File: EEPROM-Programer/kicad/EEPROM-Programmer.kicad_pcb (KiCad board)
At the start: 2 copper layers, 100 x 60 mm, 9 parts

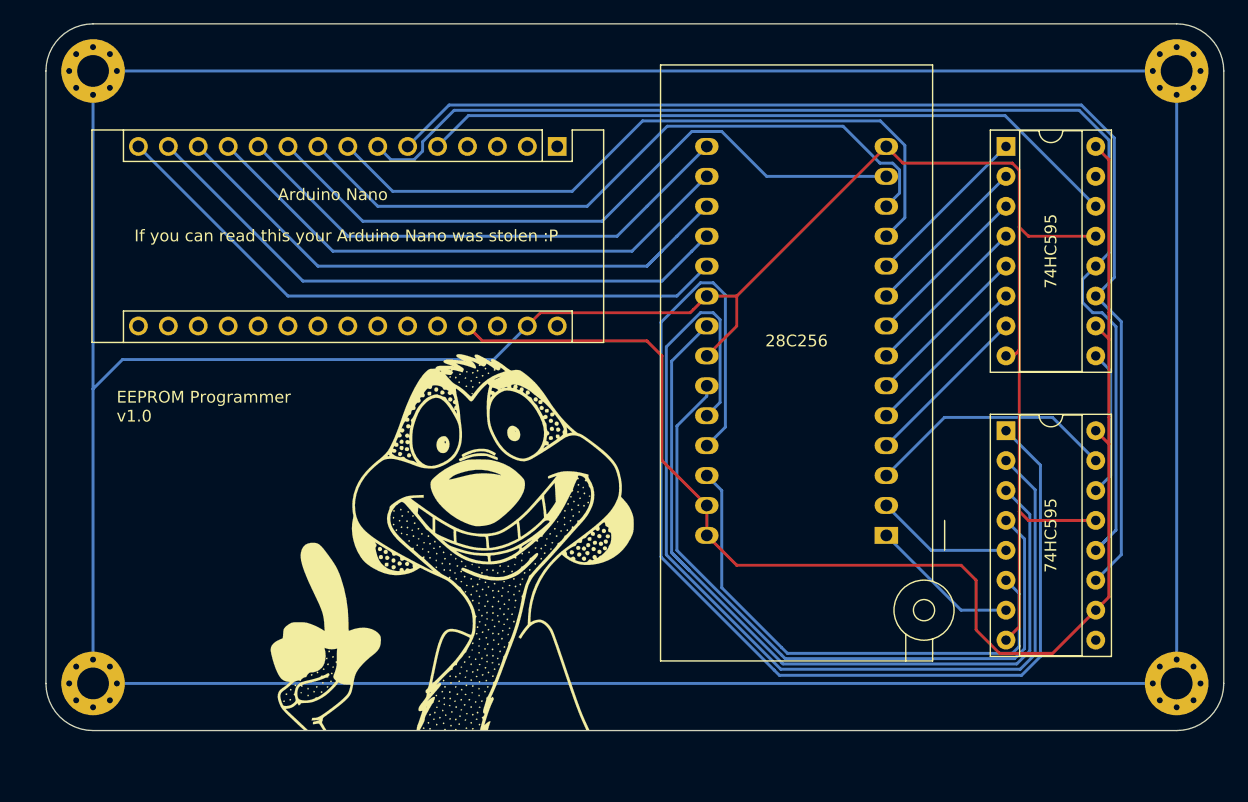
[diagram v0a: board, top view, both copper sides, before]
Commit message: EEPROM Programmer: New circuit, with more flexibility
Redesigned the circuit to be able to control the OE, CS and WE pins from the
EEPROM, and the OE, SRCLR pins from the shift register.

This gives us more total control of all the pins in both chips, and
enables us to write to the EEPROM (before the WE pin was always HIGH).

I also added a status LED for monitoring.
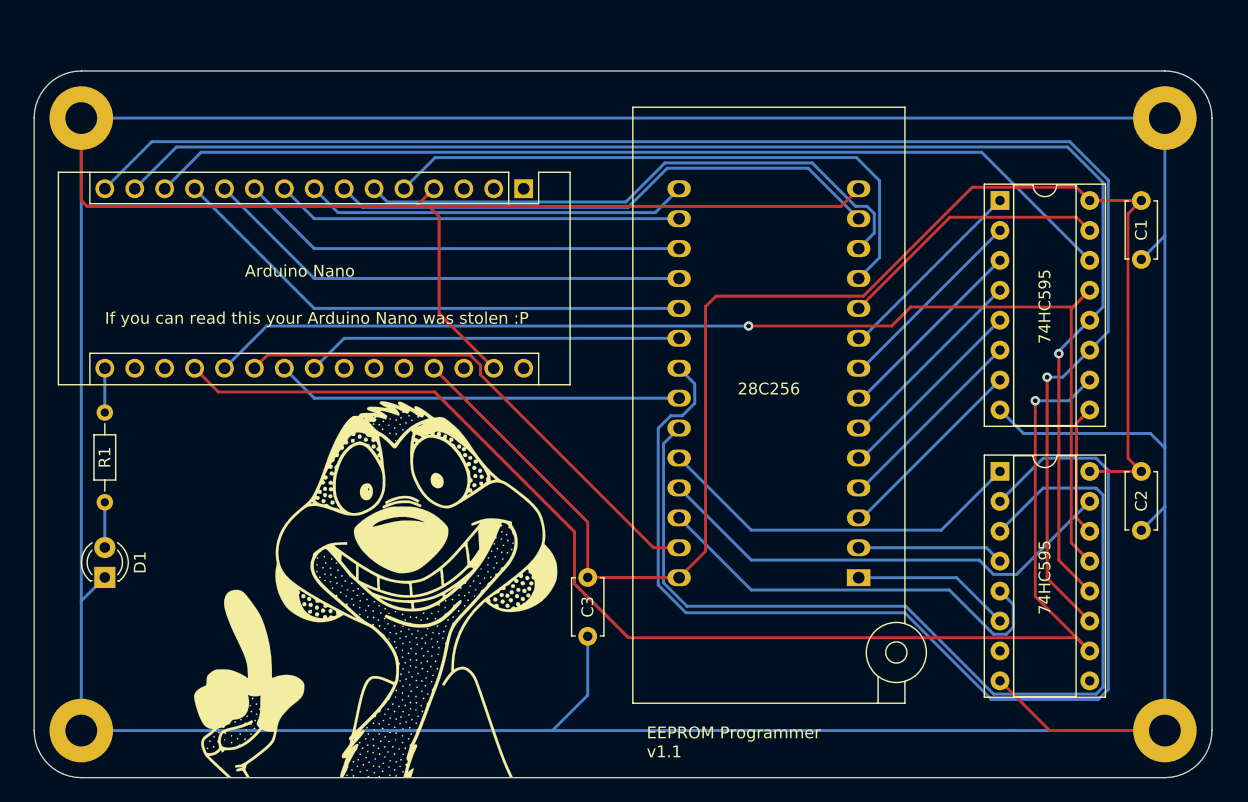
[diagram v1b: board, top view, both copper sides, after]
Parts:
- removed the 74HC595 at (179.0, 72.3)
- removed the 74HC595 at (179.0, 96.5)
- removed G***: LOGO, personalLIB:timon_31x32
- added 74HC595: 74HC595, Package_DIP:DIP-16_W7.62mm_Socket, F.Cu at (178.5, 76.9)
- added 74HC595: 74HC595, Package_DIP:DIP-16_W7.62mm_Socket, F.Cu at (178.5, 99.9)
- added C1: 100n, Capacitor_THT:C_Disc_D4.7mm_W2.5mm_P5.00mm, F.Cu at (190.5, 81.9)
- added C2: 100n, Capacitor_THT:C_Disc_D4.7mm_W2.5mm_P5.00mm, F.Cu at (190.5, 104.9)
- added C3: 100n, Capacitor_THT:C_Disc_D4.7mm_W2.5mm_P5.00mm, F.Cu at (143.5, 113.9)
- added D1: LED, LED_THT:LED_D3.0mm, F.Cu at (102.5, 108.9)
- added R1: 220, Resistor_THT:R_Axial_DIN0204_L3.6mm_D1.6mm_P7.62mm_Horizontal, F.Cu at (102.5, 94.9)
- added Timon: LOGO, personalLib:timon_31x32, F.Cu at (125.5, 109.9)
- H1, H2, H3, H4: footprint MountingHole:MountingHole_2.7mm_Pad_Via -> MountingHole:MountingHole_2.7mm_Pad
- moved Arduino Nano 4.58 mm to (138.0, 75.9)
- moved 28C256 4.29 mm to (166.5, 108.9)
- moved H1 4.12 mm to (100.5, 69.9)
- moved H2 4.12 mm to (192.5, 69.9)
- moved H3 4.12 mm to (192.5, 121.9)
- moved H4 4.12 mm to (100.5, 121.9)
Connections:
- 28C256 pad 11: Net-(A1-Pad8) -> Net-(A1-Pad5)
- 28C256 pad 12: Net-(A1-Pad9) -> Net-(A1-Pad6)
- 28C256 pad 13: Net-(A1-Pad10) -> Net-(A1-Pad7)
- 28C256 pad 15: Net-(A1-Pad11) -> Net-(A1-Pad8)
- 28C256 pad 16: Net-(A1-Pad12) -> Net-(A1-Pad9)
- 28C256 pad 17: Net-(A1-Pad13) -> Net-(A1-Pad10)
- 28C256 pad 18: Net-(A1-Pad14) -> Net-(A1-Pad11)
- 28C256 pad 19: Net-(A1-Pad15) -> Net-(A1-Pad12)
- 28C256 pad 20: GND -> Net-(A1-Pad23)
- 28C256 pad 22: GND -> Net-(A1-Pad22)
- 28C256 pad 27: VCC -> Net-(A1-Pad21)
- 28C256 pad 28: VCC -> Vcc
- Arduino Nano pad 27: VCC -> Vcc
- Arduino Nano pad 4: Net-(A1-Pad4) -> GND
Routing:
- net Vcc: track 0.00 -> 124.9 mm
- net VCC: track 119.0 -> 0.00 mm
- net Net-(A1-Pad19): track 0.00 -> 117.5 mm, vias 0 -> 1
- net Net-(A1-Pad20): track 0.00 -> 98.5 mm, vias 0 -> 1
- net Net-(A1-Pad15): track 54.6 -> 130.1 mm, vias 0 -> 1
- net Net-(A1-Pad14): track 52.0 -> 122.3 mm, vias 0 -> 1
- net Net-(A1-Pad7): track 105.5 -> 47.5 mm
- net Net-(U2-Pad15): track 98.1 -> 40.5 mm
- net Net-(U2-Pad1): track 85.6 -> 31.8 mm
- net Net-(A1-Pad6): track 102.6 -> 49.6 mm
- net Net-(A1-Pad21): track 0.00 -> 43.8 mm
- net Net-(A1-Pad22): track 0.00 -> 34.6 mm
- net Net-(A1-Pad13): track 51.3 -> 83.6 mm
- net Net-(A1-Pad23): track 0.00 -> 32.0 mm
- net Net-(A1-Pad8): track 60.6 -> 32.7 mm
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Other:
- board text added: "EEPROM Programmer v1.1"
- board text removed: "EEPROM Programmer v1.0"
